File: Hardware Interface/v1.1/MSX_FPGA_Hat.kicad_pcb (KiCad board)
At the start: 2 copper layers, 103 x 66 mm, 26 parts, among them J1 J1, J2 J2, J3a1 J3a, J3b1 J3b, J4a1 J4a, J4b1 J4b, U1 74LVC245A, U2 74LVC245A, U3 74LVC245A, U4 74LVC245A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

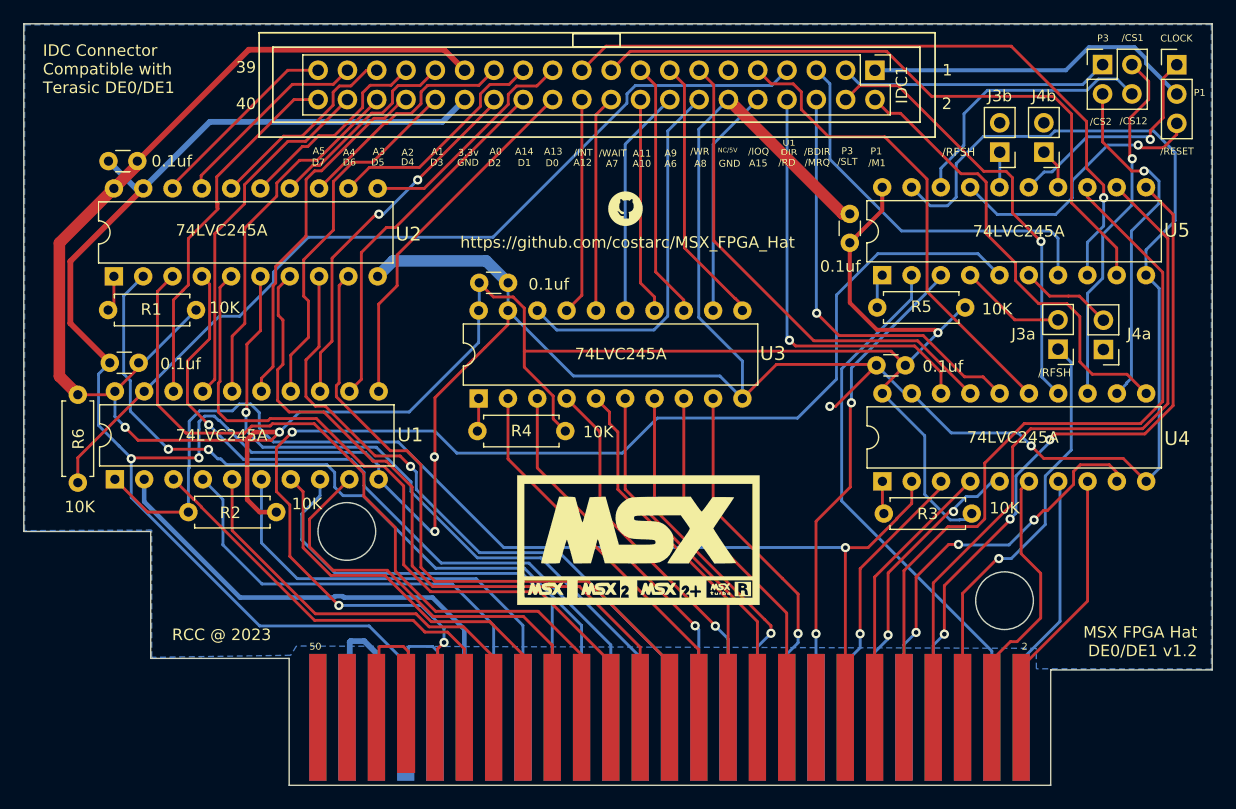
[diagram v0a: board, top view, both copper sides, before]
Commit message: Moving to version 1.2 as it's clear that the OD pin in the U1 is not being driven correctly and need a separate pin for this purpose. V1.2 has this change implemented
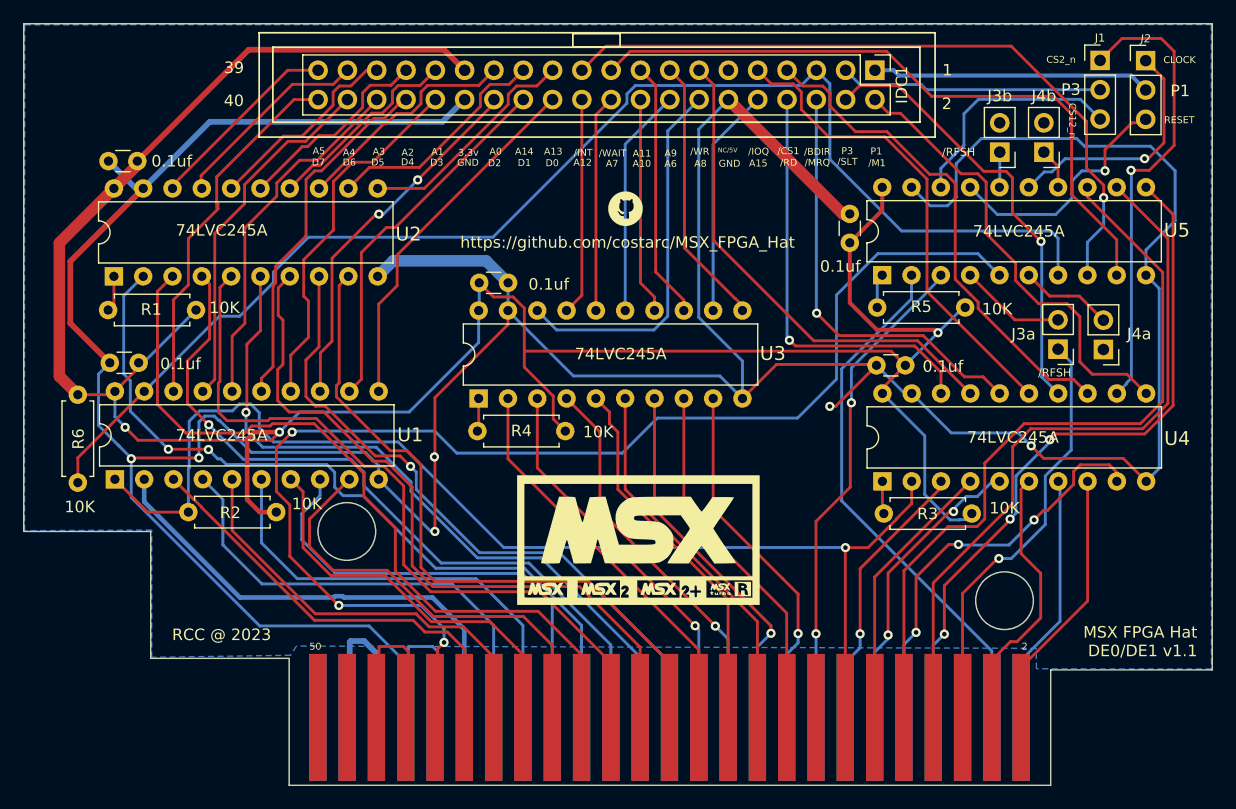
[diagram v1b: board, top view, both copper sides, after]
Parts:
- CONN1: footprint Roni Footprints:MSX_CART_SW -> Roni Footprints:MSX_CART
- J1: footprint Connector_PinHeader_2.54mm:PinHeader_2x02_P2.54mm_Vertical -> Connector_PinHeader_2.54mm:PinHeader_1x03_P2.54mm_Vertical
- moved J2 2.72 mm to (149.2, 23.4)
- moved J1 0.42 mm to (145.2, 23.4)
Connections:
- IDC1 pad 3: /C_CS_SLT -> C_CS2_CS12
- IDC1 pad 7: /C_LVC245_DIR -> /C_CS1
- J1 pad 1: /C_CS_SLT -> /C_CS2
- J1 pad 2: /C_CS1 -> C_CS2_CS12
- J1 pad 3: /C_CS2 -> /C_CS12
- R6 pad 2: /C_LVC245_DIR -> /C_BUSDIR
- U1 pad 19: /C_LVC245_DIR -> /C_BUSDIR
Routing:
- net /C_BUSDIR: track 34.0 -> 115.1 mm
- net /C_LVC245_DIR: track 78.5 -> 0.00 mm
- net /C_CS_SLT: track 23.5 -> 0.00 mm
- net C_CS2_CS12: track 0.00 -> 22.8 mm
- net /C_CS1: track 31.5 -> 43.8 mm, vias 1 -> 0
- net /C_CS2: track 30.4 -> 40.3 mm
- net C_CLK_OR_RST: track 28.9 -> 24.2 mm
- net /C_CS12: track 23.5 -> 20.2 mm
- net /C_RESET: track 23.8 -> 21.6 mm
- net GNDREF: track 359.9 -> 358.4 mm
- net C_CLOCK: track 19.9 -> 21.1 mm
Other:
- board text added: "CS12_n"
- board text added: "CS2_n"
- board text added: "MSX FPGA Hat DE0/DE1 v1.1"
- board text added: "RESET"
- board text removed: "/CS12"
- board text removed: "/CS2"
- board text removed: "/RESET"
- board text removed: "IDC Connector Compatible with Terasic DE0/DE1"
- board text removed: "MSX FPGA Hat DE0/DE1 v1.2"
- board text removed: "U1 DIR"
